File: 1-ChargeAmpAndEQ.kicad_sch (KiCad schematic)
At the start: 44 parts, among them J101 6.3mm stereo, J102 6.3mm stereo, U1 OPA145

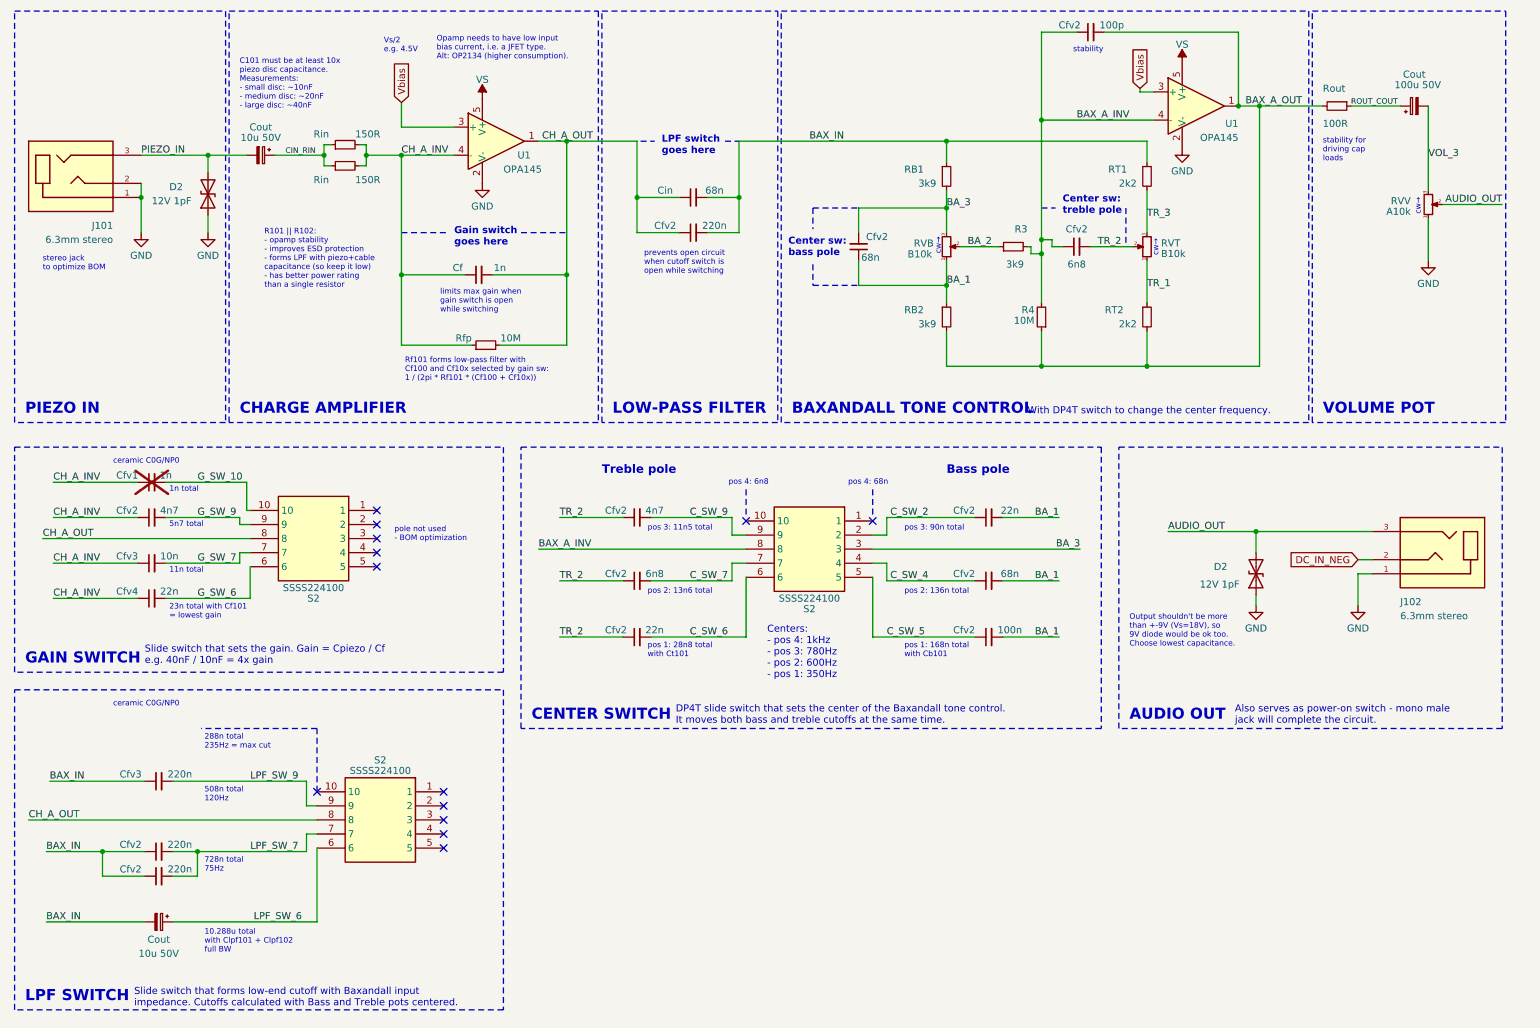
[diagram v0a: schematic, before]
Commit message: v2.2: correcting pins of audio jacks - T and R were swapped. Fixing in schematic and PCB
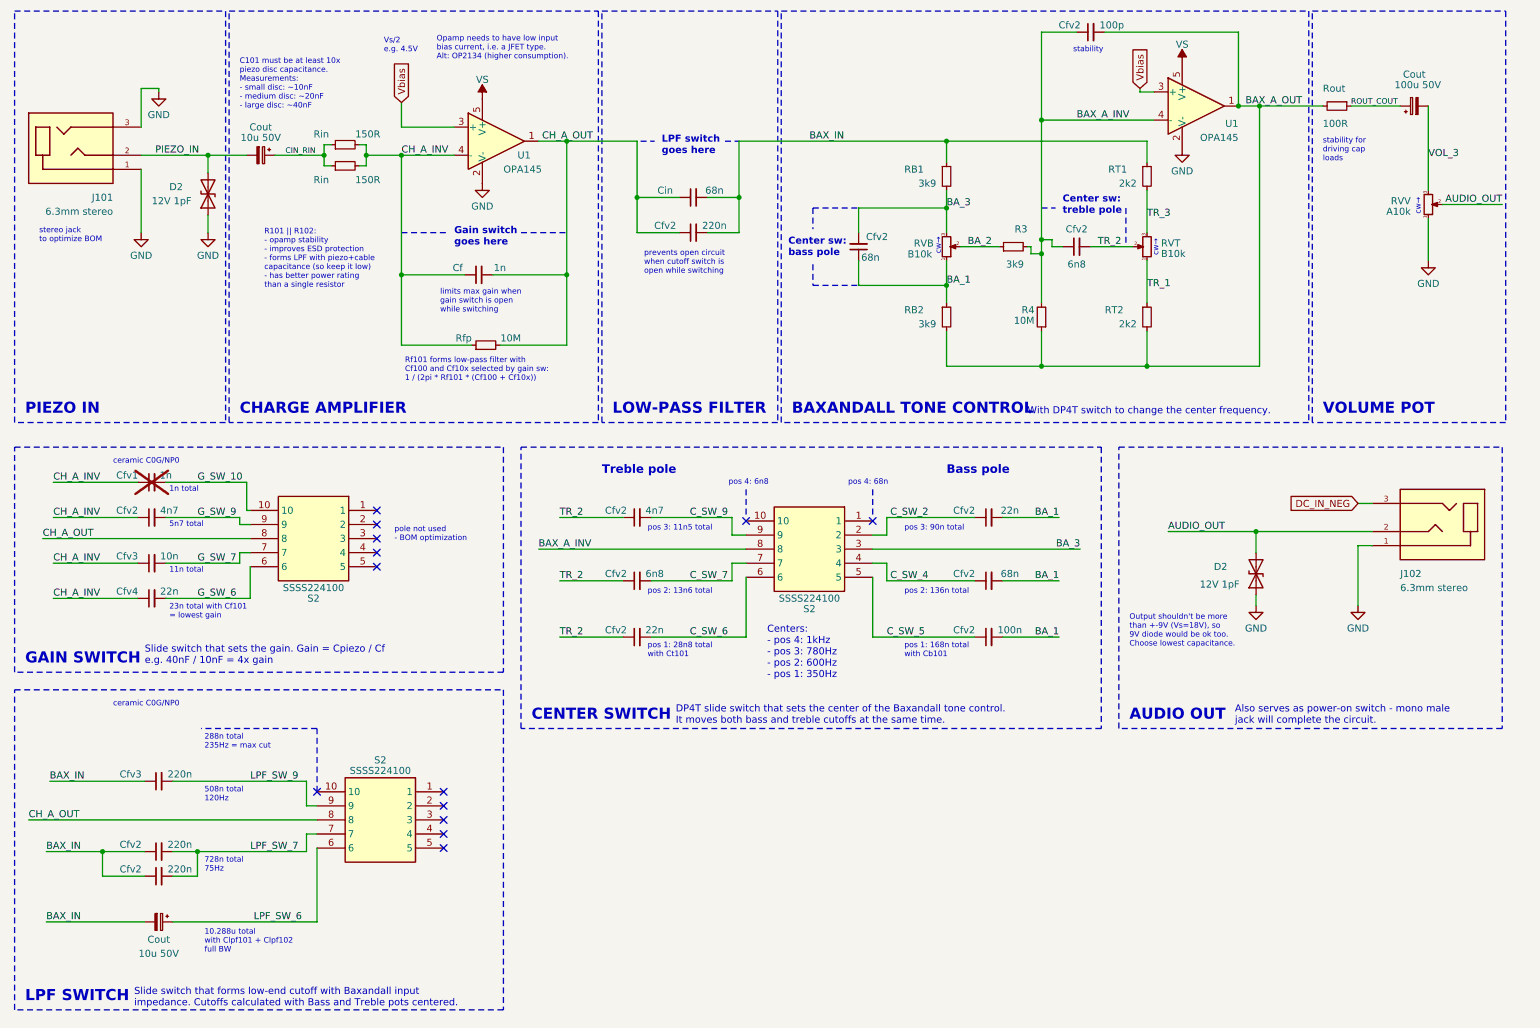
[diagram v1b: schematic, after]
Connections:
- net AUDIO_OUT: now also J102.2; no longer J102.3
- net DC_IN_NEG: now also J102.3; no longer J102.2
- net GND: now also J101.3; no longer J101.2
- net PIEZO_IN: now also J101.2; no longer J101.3
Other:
- moved on the sheet: J101, J102
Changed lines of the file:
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@@
   (title_block
     (title "Charge Amp and Baxandall EQ")
-    (date "2023-12-08")
-    (rev "2.1")
+    (date "2023-12-27")
+    (rev "2.2")
     (company "Arx")
   )
@@
   (junction (at 182.245 64.77) (diameter 0) (color 0 0 0 0)
   )
-  (junction (at 36.83 48.895) (diameter 0) (color 0 0 0 0)
-  )
   (junction (at 238.125 109.22) (diameter 0) (color 0 0 0 0)
   )
@@
     (stroke (width 0) (type dot))
   )
-  (wire (pts (xy 256.54 116.84) (xy 259.08 116.84))
+  (wire (pts (xy 36.83 29.21) (xy 40.005 29.21))
     (stroke (width 0) (type default))
   )
@@
     (stroke (width 0) (type default))
   )
-  (wire (pts (xy 54.61 113.03) (xy 56.515 113.03))
+  (wire (pts (xy 36.83 41.275) (xy 48.895 41.275))
     (stroke (width 0) (type default))
   )
-  (wire (pts (xy 36.83 41.275) (xy 48.895 41.275))
+  (wire (pts (xy 54.61 113.03) (xy 56.515 113.03))
     (stroke (width 0) (type default))
   )
@@
     (stroke (width 0) (type default))
   )
-  (wire (pts (xy 36.83 48.895) (xy 36.83 55.245))
+  (wire (pts (xy 16.51 161.29) (xy 68.58 161.29))
     (stroke (width 0) (type default))
   )
-  (wire (pts (xy 16.51 161.29) (xy 68.58 161.29))
+  (wire (pts (xy 36.83 36.195) (xy 36.83 29.21))
     (stroke (width 0) (type default))
   )
@@
     (stroke (width 0) (type default))
   )
-  (wire (pts (xy 256.54 122.555) (xy 256.54 116.84))
+  (wire (pts (xy 256.54 111.76) (xy 256.54 122.555))
     (stroke (width 0) (type default))
   )
@@
     (stroke (width 0) (type default))
   )
+  (wire (pts (xy 40.005 29.21) (xy 40.005 29.845))
+    (stroke (width 0) (type default))
+  )
   (wire (pts (xy 48.895 41.275) (xy 48.895 44.45))
     (stroke (width 0) (type default))
@@
     (stroke (width 0) (type default))
   )
+  (wire (pts (xy 256.54 111.76) (xy 259.08 111.76))
+    (stroke (width 0) (type default))
+  )
   (wire (pts (xy 56.515 115.57) (xy 56.515 121.285))
     (stroke (width 0) (type default))
@@
     (stroke (width 0) (type default))
   )
-  (wire (pts (xy 256.54 114.3) (xy 259.08 114.3))
+  (wire (pts (xy 256.54 104.14) (xy 259.08 104.14))
     (stroke (width 0) (type default))
   )
@@
     (stroke (width 0) (type default))
   )
-  (wire (pts (xy 36.83 46.355) (xy 36.83 48.895))
+  (wire (pts (xy 36.83 43.815) (xy 36.83 55.245))
     (stroke (width 0) (type default))
   )
@@
     (fill (type none))
   )
-  (text "stereo jack \nto optimize BOM" (at 19.05 62.23 0)
+  (text "stereo jack \nto optimize BOM" (at 18.415 57.15 0)
     (effects (font (size 1 1)) (justify left bottom))
   )
@@
     (effects (font (size 1.27 1.27)) (justify left bottom))
   )
-  (label "PIEZO_IN" (at 36.83 41.275 0) (fields_autoplaced)
+  (label "PIEZO_IN" (at 39.37 41.275 0) (fields_autoplaced)
     (effects (font (size 1.27 1.27)) (justify left bottom))
   )
@@
     )
   )
-  (global_label "DC_IN_NEG" (shape input) (at 256.54 114.3 180) (fields_autoplaced)
+  (global_label "DC_IN_NEG" (shape input) (at 256.54 104.14 180) (fields_autoplaced)
     (effects (font (size 1.27 1.27)) (justify right))
-    (property "Intersheetrefs" "${INTERSHEET_REFS}" (at 243.4742 114.3 0)
+    (property "Intersheetrefs" "${INTERSHEET_REFS}" (at 243.4742 104.14 0)
       (effects (font (size 1.27 1.27)) (justify right) hide)
     )
@@
       (effects (font (size 1.27 1.27)) (justify left top) hide)
     )
-    (property "Datasheet" "https://www.alps.com/prod/info/E/HTML/Switch/Slide/SSSS2/SSSS224100.html" (at 60.325 300.33 0)
+    (property "Datasheet" "https://tech.alpsalpine.com/e/products/detail/SSSS224100/" (at 60.325 300.33 0)
       (effects (font (size 1.27 1.27)) (justify left top) hide)
     )
@@
     )
   )
-  (symbol (lib_id "CUI_SJ-63053A:SJ-63053A") (at 24.13 46.355 0) (mirror x) (unit 1)
+  (symbol (lib_id "CUI_SJ-63053A:SJ-63053A") (at 24.13 41.275 0) (mirror x) (unit 1)
     (in_bom yes) (on_board yes) (dnp no)
-    (property "Reference" "J101" (at 31.75 53.975 0)
+    (property "Reference" "J101" (at 31.75 48.895 0)
       (effects (font (size 1.27 1.27)) (justify right))
     )
-    (property "Value" "6.3mm stereo" (at 31.75 56.515 0)
+    (property "Value" "6.3mm stereo" (at 31.75 51.435 0)
       (effects (font (size 1.27 1.27)) (justify right))
     )
-    (property "Footprint" "library:CUI_SJ-63053A" (at 24.13 46.355 0)
+    (property "Footprint" "library:CUI_SJ-63053A" (at 24.13 41.275 0)
       (effects (font (size 1.27 1.27)) hide)
     )
-    (property "Datasheet" "https://cz.mouser.com/datasheet/2/670/sj_63053b-1903437.pdf" (at 24.13 46.355 0)
+    (property "Datasheet" "https://cz.mouser.com/datasheet/2/670/sj_63053b-1903437.pdf" (at 24.13 41.275 0)
       (effects (font (size 1.27 1.27)) hide)
     )
-    (property "Purpose" "input piezo jack" (at 24.13 46.355 0)
+    (property "Purpose" "input piezo jack" (at 24.13 41.275 0)
       (effects (font (size 1.27 1.27)) hide)
     )
-    (property "LCSC Part #" "-" (at 24.13 46.355 0)
+    (property "LCSC Part #" "-" (at 24.13 41.275 0)
       (effects (font (size 1.27 1.27)) hide)
     )
-    (property "Mfr" "CUI Devices" (at 24.13 46.355 0)
+    (property "Mfr" "CUI Devices" (at 24.13 41.275 0)
       (effects (font (size 1.27 1.27)) hide)
     )
-    (property "Mfr Part #" "SJ-63053A" (at 24.13 46.355 0)
+    (property "Mfr Part #" "SJ-63053A" (at 24.13 41.275 0)
       (effects (font (size 1.27 1.27)) hide)
     )
-    (property "Mouser Part #" "490-SJ-63053A" (at 24.13 46.355 0)
+    (property "Mouser Part #" "490-SJ-63053A" (at 24.13 41.275 0)
       (effects (font (size 1.27 1.27)) hide)
     )
-    (property "TME Part #" "-" (at 24.13 46.355 0)
+    (property "TME Part #" "-" (at 24.13 41.275 0)
       (effects (font (size 1.27 1.27)) hide)
     )
@@
     )
   )
-  (symbol (lib_id "CUI_SJ-63053A:SJ-63053A") (at 271.78 114.3 180) (unit 1)
+  (symbol (lib_id "CUI_SJ-63053A:SJ-63053A") (at 271.78 109.22 180) (unit 1)
     (in_bom yes) (on_board yes) (dnp no)
-    (property "Reference" "J102" (at 264.16 121.92 0)
+    (property "Reference" "J102" (at 264.16 116.84 0)
       (effects (font (size 1.27 1.27)) (justify right))
     )
-    (property "Value" "6.3mm stereo" (at 264.16 124.46 0)
+    (property "Value" "6.3mm stereo" (at 264.16 119.38 0)
       (effects (font (size 1.27 1.27)) (justify right))
     )
-    (property "Footprint" "library:CUI_SJ-63053A" (at 271.78 114.3 0)
+    (property "Footprint" "library:CUI_SJ-63053A" (at 271.78 109.22 0)
       (effects (font (size 1.27 1.27)) hide)
     )
-    (property "Datasheet" "https://cz.mouser.com/datasheet/2/670/sj_63053b-1903437.pdf" (at 271.78 114.3 0)
+    (property "Datasheet" "https://cz.mouser.com/datasheet/2/670/sj_63053b-1903437.pdf" (at 271.78 109.22 0)
       (effects (font (size 1.27 1.27)) hide)
     )
-    (property "Purpose" "output audio jack" (at 271.78 114.3 0)
+    (property "Purpose" "output audio jack" (at 271.78 109.22 0)
       (effects (font (size 1.27 1.27)) hide)
     )
-    (property "LCSC Part #" "-" (at 271.78 114.3 0)
+    (property "LCSC Part #" "-" (at 271.78 109.22 0)
       (effects (font (size 1.27 1.27)) hide)
     )
-    (property "Mfr" "CUI Devices" (at 271.78 114.3 0)
+    (property "Mfr" "CUI Devices" (at 271.78 109.22 0)
       (effects (font (size 1.27 1.27)) hide)
     )
-    (property "Mfr Part #" "SJ-63053A" (at 271.78 114.3 0)
+    (property "Mfr Part #" "SJ-63053A" (at 271.78 109.22 0)
       (effects (font (size 1.27 1.27)) hide)
     )
-    (property "Mouser Part #" "490-SJ-63053A" (at 271.78 114.3 0)
+    (property "Mouser Part #" "490-SJ-63053A" (at 271.78 109.22 0)
       (effects (font (size 1.27 1.27)) hide)
     )
-    (property "TME Part #" "-" (at 271.78 114.3 0)
+    (property "TME Part #" "-" (at 271.78 109.22 0)
       (effects (font (size 1.27 1.27)) hide)
     )
@@
       (effects (font (size 1.27 1.27)) (justify left top) hide)
     )
-    (property "Datasheet" "https://www.alps.com/prod/info/E/HTML/Switch/Slide/SSSS2/SSSS224100.html" (at 149.86 302.235 0)
+    (property "Datasheet" "https://tech.alpsalpine.com/e/products/detail/SSSS224100/" (at 149.86 302.235 0)
       (effects (font (size 1.27 1.27)) (justify left top) hide)
     )
@@
       (effects (font (size 1.27 1.27)) (justify left top) hide)
     )
-    (property "Datasheet" "https://www.alps.com/prod/info/E/HTML/Switch/Slide/SSSS2/SSSS224100.html" (at 72.39 351.13 0)
+    (property "Datasheet" "https://tech.alpsalpine.com/e/products/detail/SSSS224100/" (at 72.39 351.13 0)
       (effects (font (size 1.27 1.27)) (justify left top) hide)
     )
@@
         )
       )
+    )
+  )
+  (symbol (lib_id "power:GND") (at 40.005 29.845 0) (unit 1)
+    (in_bom yes) (on_board yes) (dnp no) (fields_autoplaced)
+    (property "Reference" "#PWR030" (at 40.005 36.195 0)
+      (effects (font (size 1.27 1.27)) hide)
+    )
+    (property "Value" "GND" (at 40.005 33.9805 0)
+      (effects (font (size 1.27 1.27)))
+    )
+    (property "Footprint" "" (at 40.005 29.845 0)
+      (effects (font (size 1.27 1.27)) hide)
+    )
+    (property "Datasheet" "" (at 40.005 29.845 0)
+      (effects (font (size 1.27 1.27)) hide)
+    )
+    (pin "1")
+    (instances
+      (project "2023_PiezoPreamp"
+        (path "/6e141482-2809-49ad-b316-4cdedc98ad26/22efb792-a214-4fa2-af90-c218e40ee577"
+          (reference "#PWR030") (unit 1)
+        )
+      )

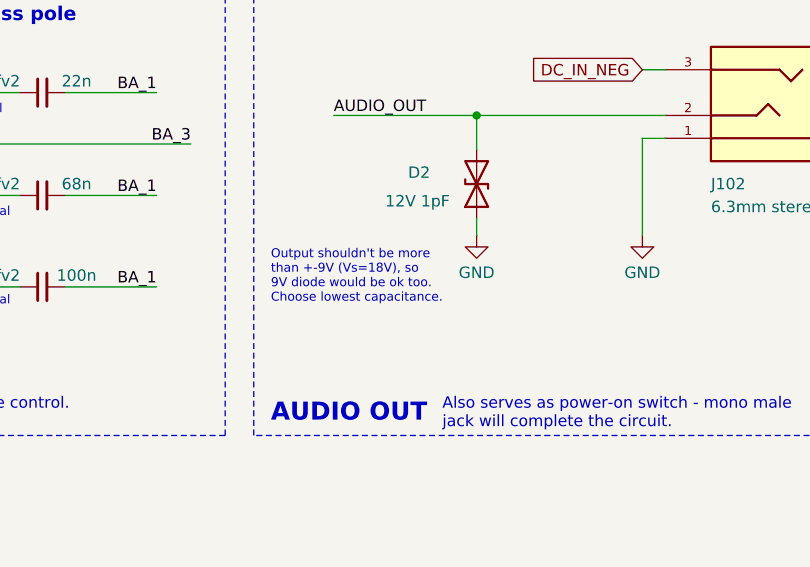
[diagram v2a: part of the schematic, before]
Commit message: Schematic: improving comments about ESD protection
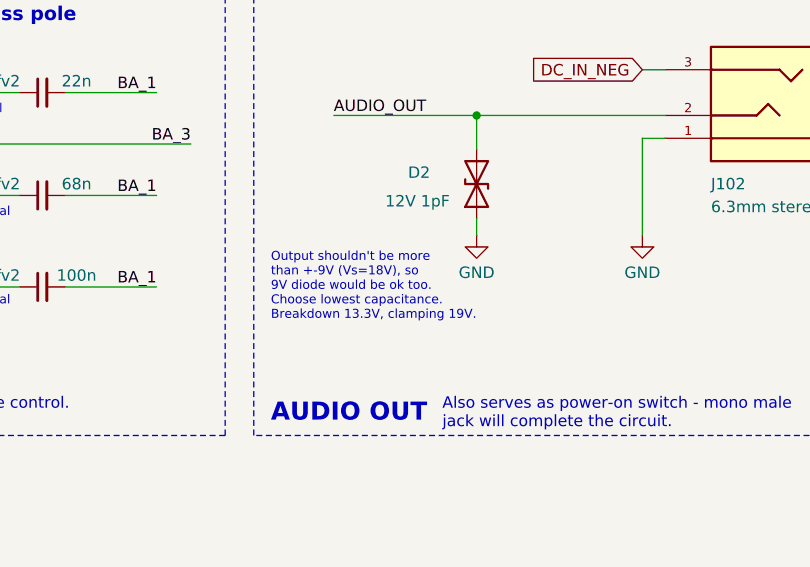
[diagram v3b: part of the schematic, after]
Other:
- note added: "Output shouldn't be more than +-9V (Vs=18V), so 9V diode would be ok too. Choose lowest capacitance. Breakdown 13.3V, clamping 19V."
- note removed: "Output shouldn't be more than +-9V (Vs=18V), so 9V diode would be ok too. Choose lowest capacitance."
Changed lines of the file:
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@@
     (effects (font (size 1 1)) (justify left bottom))
   )
-  (text "Output shouldn't be more \nthan +-9V (Vs=18V), so \n9V diode would be ok too.\nChoose lowest capacitance.\n"
-    (at 215.265 130.175 0)
+  (text "Output shouldn't be more \nthan +-9V (Vs=18V), so \n9V diode would be ok too.\nChoose lowest capacitance.\nBreakdown 13.3V, clamping 19V.\n"
+    (at 215.265 132.08 0)
     (effects (font (size 1 1)) (justify left bottom))
   )
